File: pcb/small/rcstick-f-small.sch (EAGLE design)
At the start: 41 parts, among them J1 MOLEX_48037-0001, J2 2212S, SW1 SKRPACE010, U1 STM32F042KT, U2 CC2500, U3 MCP1703AT-3302E/CB, X1 8MHz/15pF, X2 26MHz/9pF, X3 (50 Ohm)

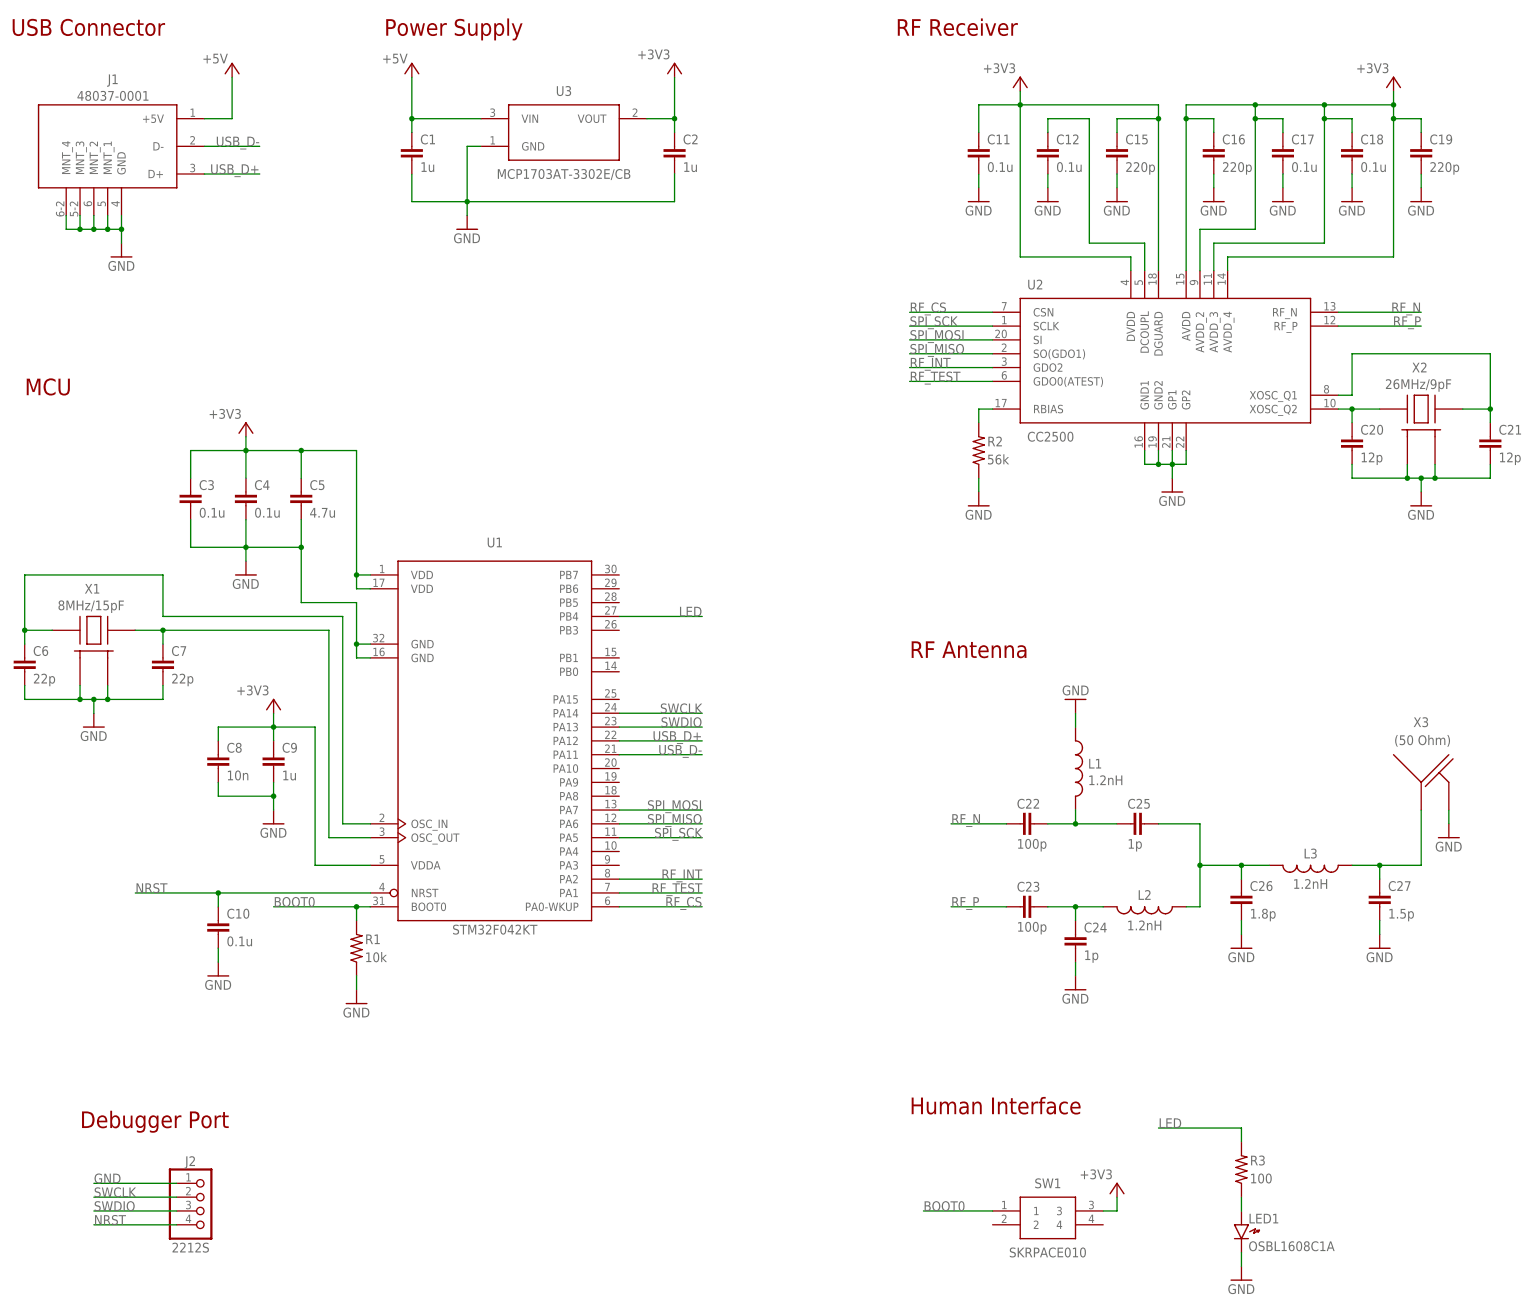
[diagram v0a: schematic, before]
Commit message: renumbering capacities
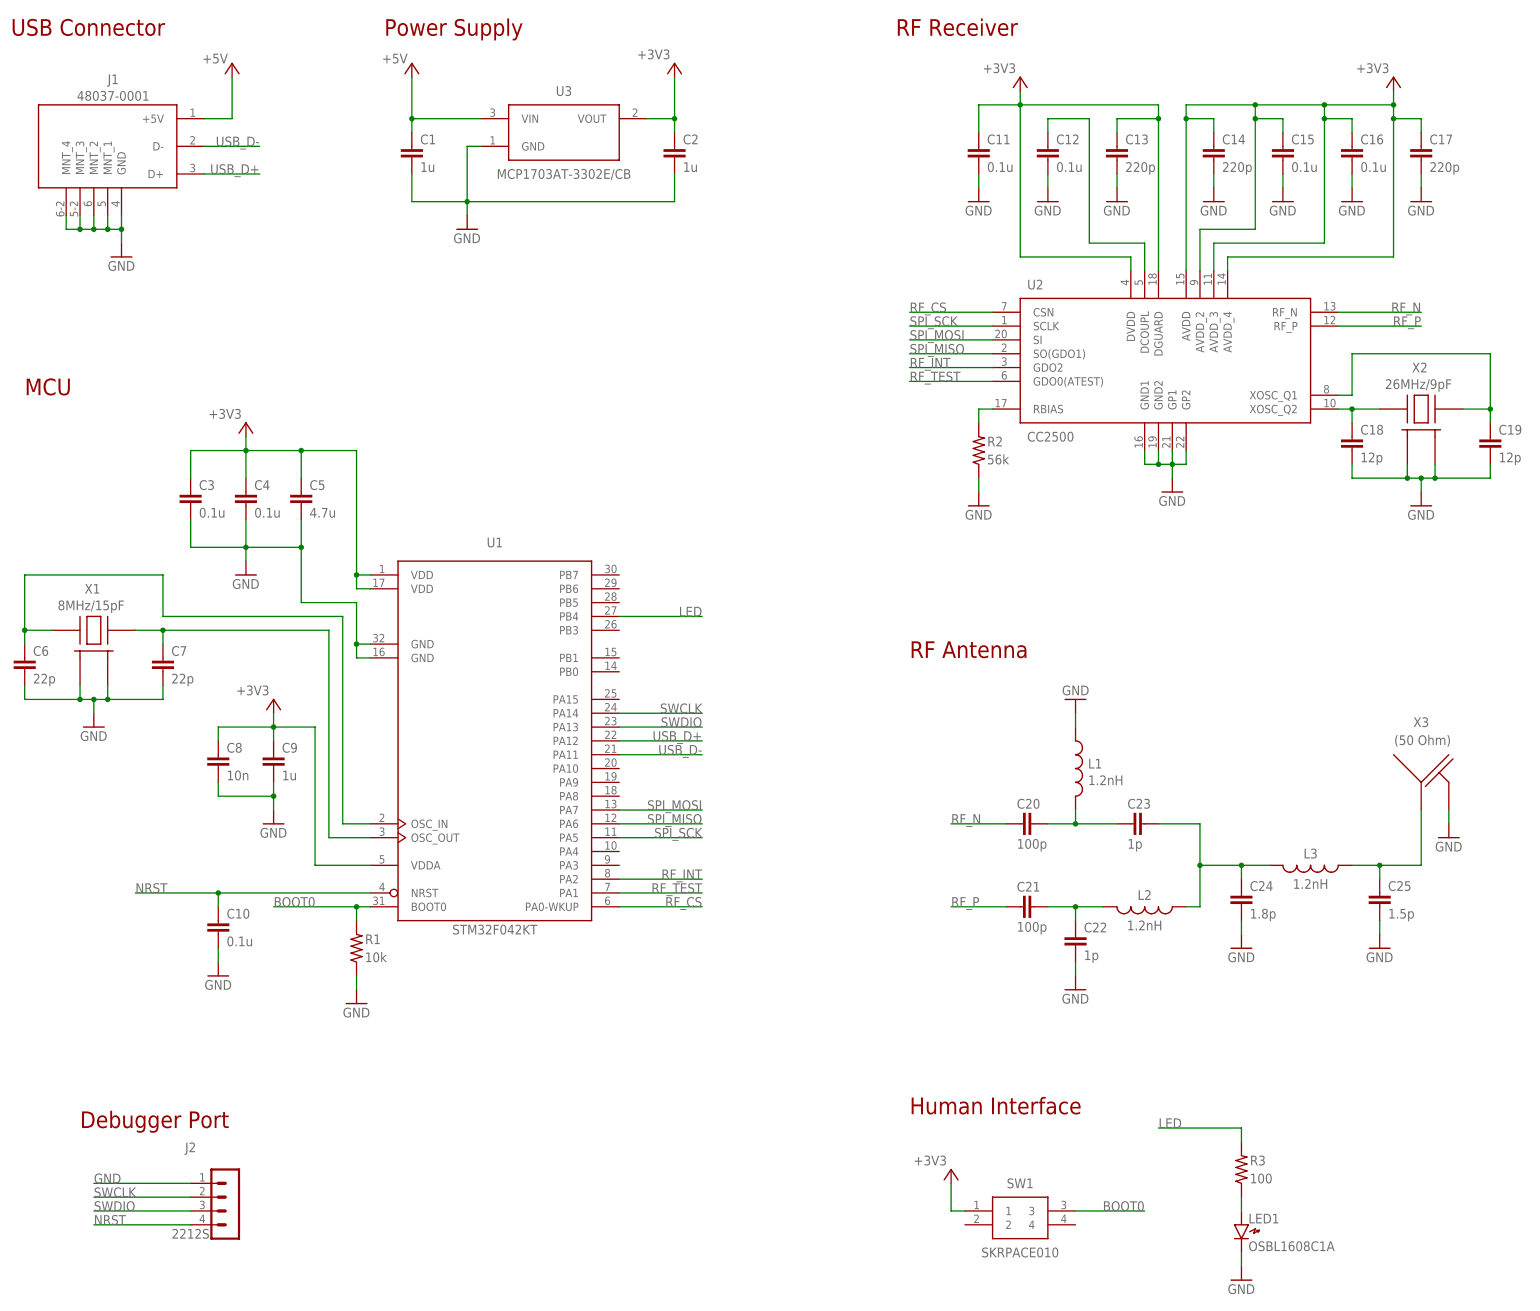
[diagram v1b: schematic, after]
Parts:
- removed C26: 1.8p, gen-discrete3:RCL_C-EUC0402-HS
- removed C27: 1.5p, gen-discrete3:RCL_C-EUC0402-HS
- added C13, C14: 220p, gen-discrete3:RCL_C-EUC0402-HS
- C15, C16: value 220p -> 0.1u
- C17: value 0.1u -> 220p
- C18: value 0.1u -> 12p
- C19: value 220p -> 12p
- C20, C21: value 12p -> 100p
- C22, C23: value 100p -> 1p
- C24: value 1p -> 1.8p
- C25: value 1p -> 1.5p
- J2: device connector2:CONNECTOR_STD-PINHD-1X4 -> connector:53047-0410
- X3: device antenna:2.4GHZ-INVERED-FLARGE-FLIP -> antenna:2.4GHZ-INVERED-FSMALL-FLIP
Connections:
- net +3V3: now also C13.1, C14.1, SW1.1; no longer C18.1, C19.1, SW1.3
- net BOOT0: now also SW1.3; no longer SW1.1
- net GND: now also C13.2, C14.2, C22.2, C25.2; no longer C20.2, C21.2, C26.2, C27.2
- net N$10: now also C23.2, C24.1; no longer C25.2, C26.1
- net N$11: now also C25.1; no longer C27.1
- net N$5: now also C20.2, C23.1; no longer C22.2, C25.1
- net N$9: now also C21.2, C22.1; no longer C23.2, C24.1
- net RF_N: now also C20.1; no longer C22.1
- net RF_P: now also C21.1; no longer C23.1
- net XOSC1: now also C19.1; no longer C21.1
- net XOSC2: now also C18.1; no longer C20.1
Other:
- moved on the sheet: C15, C16, C17, C18, C19, C20, C21, C22, C23, C24, C25, J2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

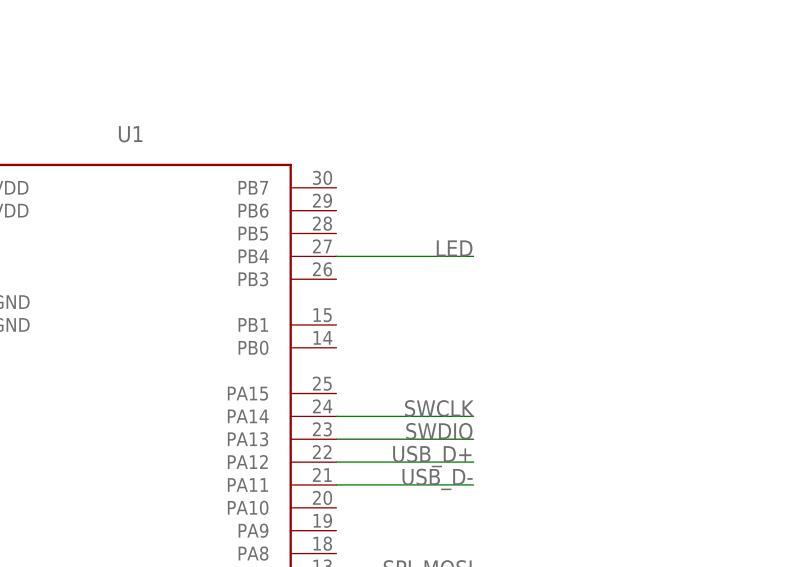
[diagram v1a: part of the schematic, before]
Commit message: refine wiring
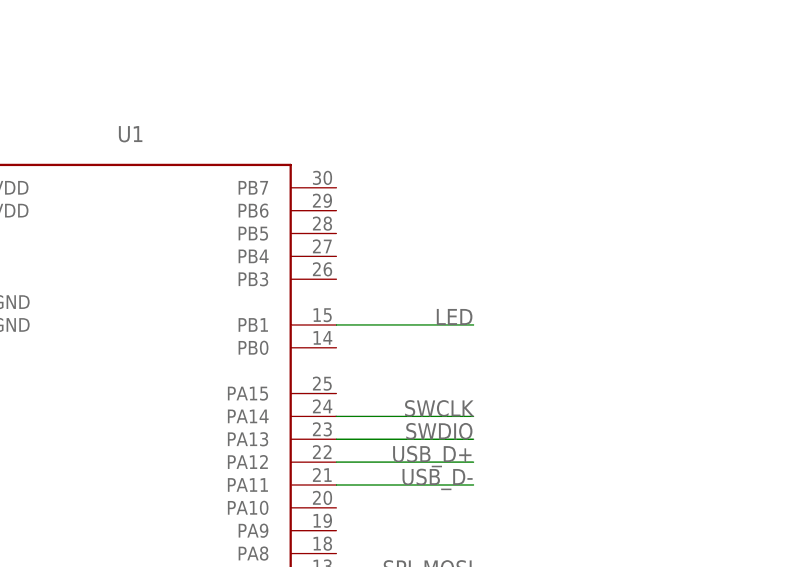
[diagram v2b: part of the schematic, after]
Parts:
- J1: device Molex - 48037-0001:MOLEX_48037-0001 -> Molex-48037-0001:MOLEX_48037-0001
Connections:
- net LED: now also U1.PB1; no longer U1.PB4
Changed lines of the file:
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@@
 </classes>
 <parts>
-<part name="J1" library="Molex - 48037-0001" library_urn="urn:adsk.eagle:library:8949197" deviceset="MOLEX_48037-0001" device="" package3d_urn="urn:adsk.eagle:package:8949201/2"/>
+<part name="J1" library="Molex-48037-0001" library_urn="urn:adsk.eagle:library:9157828" deviceset="MOLEX_48037-0001" device="" package3d_urn="urn:adsk.eagle:package:9157833/2"/>
 <part name="P+1" library="supply1" library_urn="urn:adsk.eagle:library:371" deviceset="+5V" device=""/>
 <part name="GND1" library="supply1" library_urn="urn:adsk.eagle:library:371" deviceset="GND" device=""/>
@@
 <net name="LED" class="0">
 <segment>
-<pinref part="U1" gate="G$1" pin="PB4"/>
-<wire x1="121.92" y1="127" x2="137.16" y2="127" width="0.1524" layer="91"/>
-<label x="137.16" y="127" size="1.778" layer="95" rot="MR0"/>
-</segment>
-<segment>
 <pinref part="R3" gate="G$1" pin="2"/>
 <wire x1="236.22" y1="30.48" x2="236.22" y2="33.02" width="0.1524" layer="91"/>
@@
 <label x="220.98" y="33.02" size="1.778" layer="95"/>
 </segment>
-</net>
+<segment>
+<pinref part="U1" gate="G$1" pin="PB1"/>
+<wire x1="121.92" y1="119.38" x2="137.16" y2="119.38" width="0.1524" layer="91"/>
+<label x="137.16" y="119.38" size="1.778" layer="95" rot="MR0"/>
+</segment>
+</net>

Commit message: minor update
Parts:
- X1: value 8MHz/15pF -> 16MHz/10pF
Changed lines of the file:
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@@
 <part name="C17" library="gen-discrete3" library_urn="urn:adsk.eagle:library:8961849" deviceset="RCL_C-EU" device="C0402-HS" package3d_urn="urn:adsk.eagle:package:8961862/2" value="220p"/>
 <part name="GND16" library="supply1" library_urn="urn:adsk.eagle:library:371" deviceset="GND" device=""/>
-<part name="X1" library="CRYSTAL3225" library_urn="urn:adsk.eagle:library:8815235" deviceset="CRYSTAL3225" device="HS" package3d_urn="urn:adsk.eagle:package:8815239/2" value="8MHz/15pF"/>
+<part name="X1" library="CRYSTAL3225" library_urn="urn:adsk.eagle:library:8815235" deviceset="CRYSTAL3225" device="HS" package3d_urn="urn:adsk.eagle:package:8815239/2" value="16MHz/10pF"/>
 <part name="C18" library="gen-discrete3" library_urn="urn:adsk.eagle:library:8961849" deviceset="RCL_C-EU" device="C0402-HS" package3d_urn="urn:adsk.eagle:package:8961862/2" value="12p"/>
 <part name="C19" library="gen-discrete3" library_urn="urn:adsk.eagle:library:8961849" deviceset="RCL_C-EU" device="C0402-HS" package3d_urn="urn:adsk.eagle:package:8961862/2" value="12p"/>
